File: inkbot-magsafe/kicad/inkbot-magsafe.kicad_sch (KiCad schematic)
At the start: 48 parts, among them J1 Panel FPC, U1 nRF52832-QFaa, U3 TPS22810DRV, U4 MIC5504-3.3, U5 BQ51050BRHL, Y1 32.768kHz, Y2 32MHz

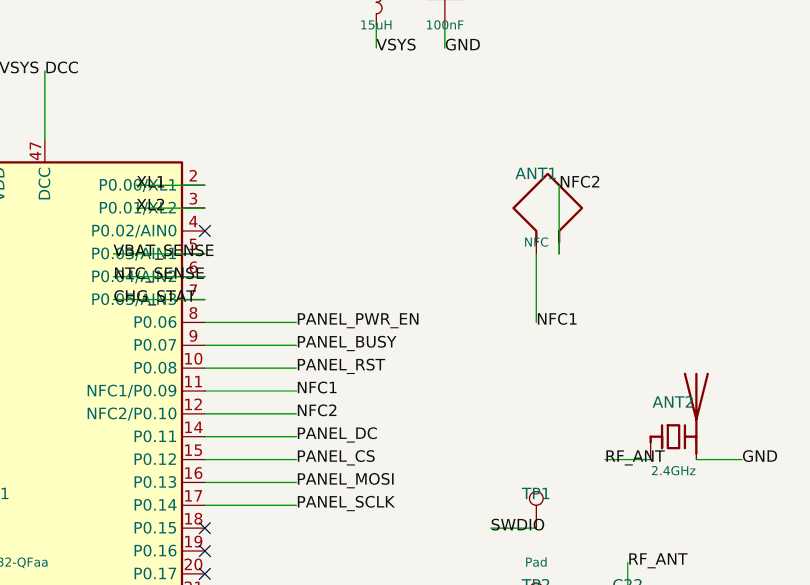
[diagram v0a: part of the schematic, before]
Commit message: inkbot-magsafe: drop NFC — pairing and frames are BLE-only
Remove the optional NFC loop antenna and free the nRF NFCT pins. Tap-to-pair
was never needed; BLE already carries pairing and the frame stream.

Co-authored-by: Jason Hall <imjasonh@users.noreply.github.com>
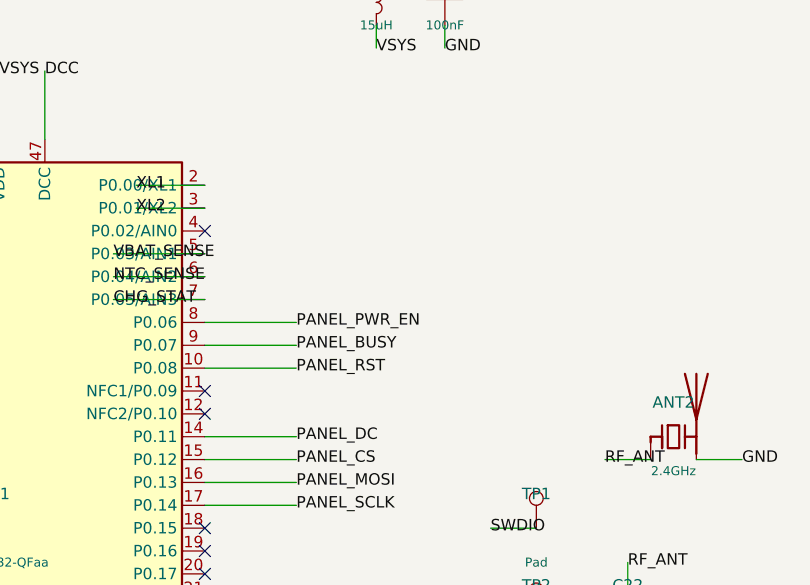
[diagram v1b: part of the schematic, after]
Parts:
- removed ANT1: NFC, symbol Device:Antenna_Loop
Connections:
- net NFC1: no longer names the net of U1.11 (NFC1/P0.09)
- net NFC2: no longer names the net of U1.12 (NFC2/P0.10)
- no-connect marks 17 -> 19

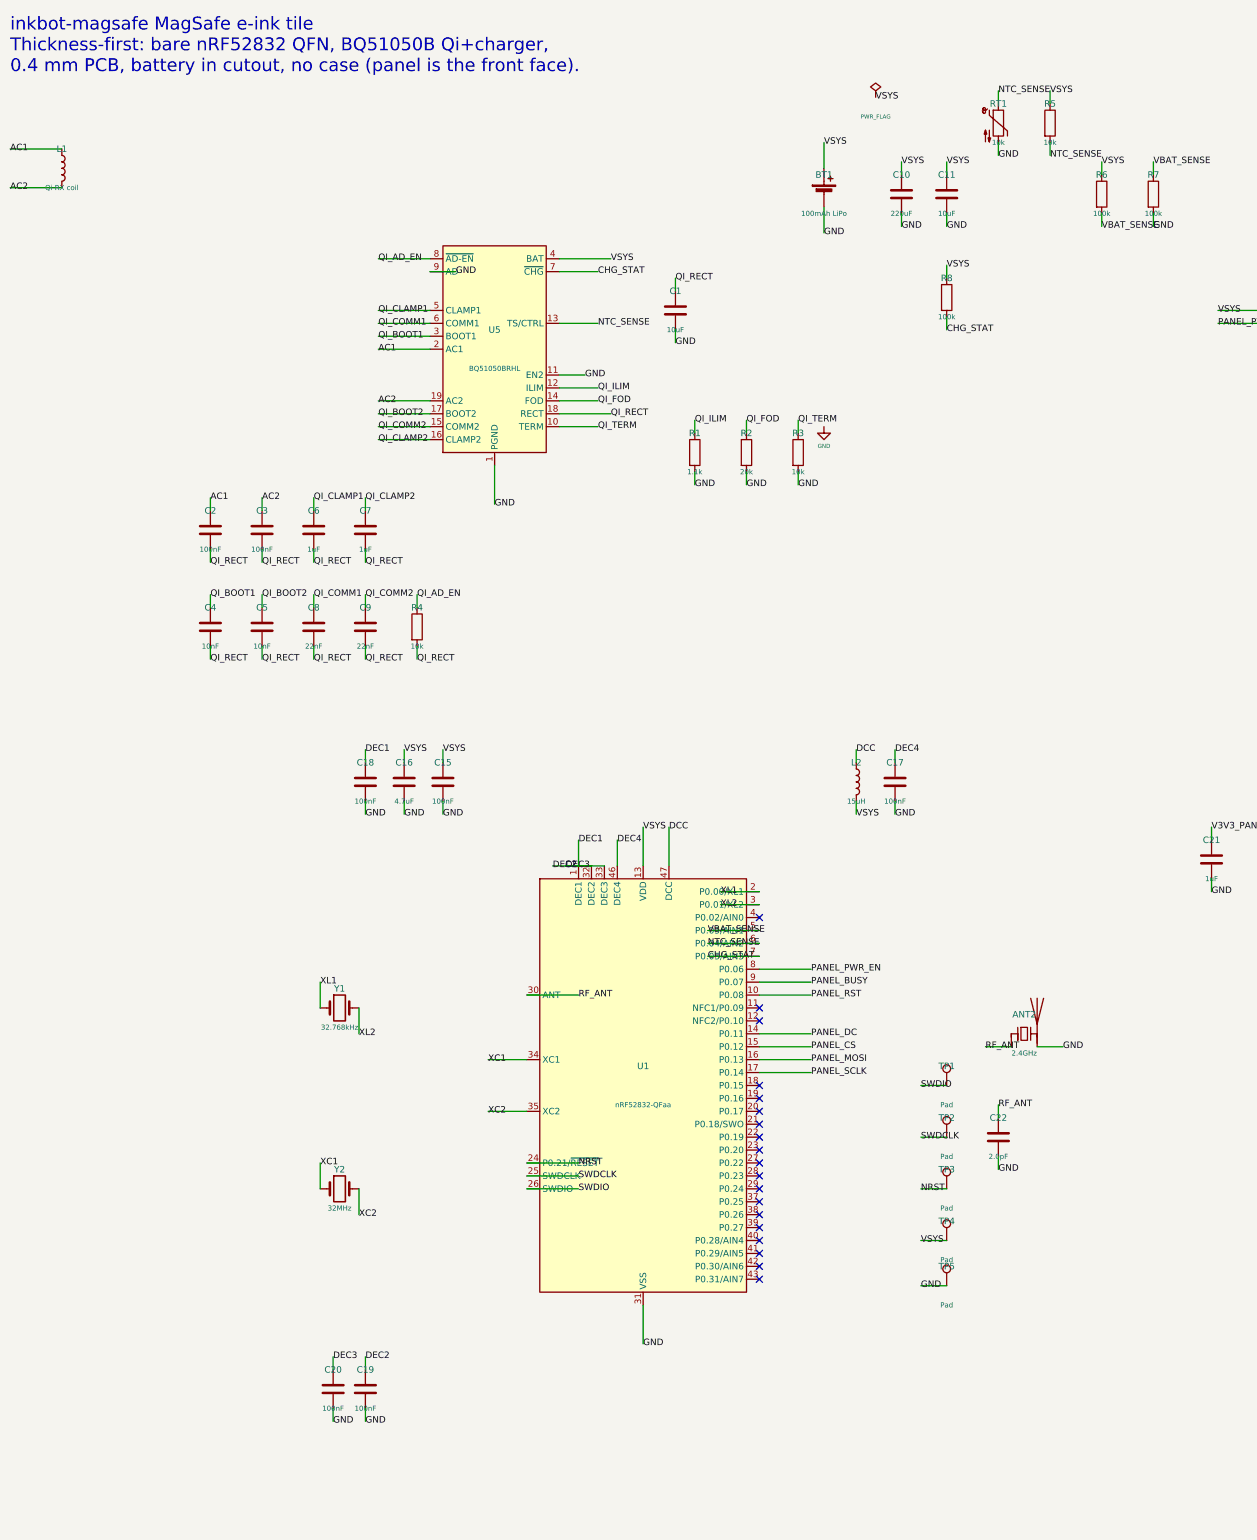
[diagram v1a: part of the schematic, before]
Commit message: inkbot-magsafe: 4.26in 480x800 panel + nRF52833; drop mini support
Maximize display for standard/Pro iPhones (minis dropped). Switch the panel to
the 4.26in GDEY0426T82 (480x800, SSD1677) — the largest mono e-paper that fits a
70.6mm iPhone in portrait — and the MCU to the nRF52833 (128KB RAM) to hold the
48KB framebuffer. Rework the schematic (QFN-40 pinout, verified netlist), the
board outline (66x108mm), firmware panel geometry, BOM, and docs. Add a phone
compatibility table to the design doc.

Co-authored-by: Jason Hall <imjasonh@users.noreply.github.com>
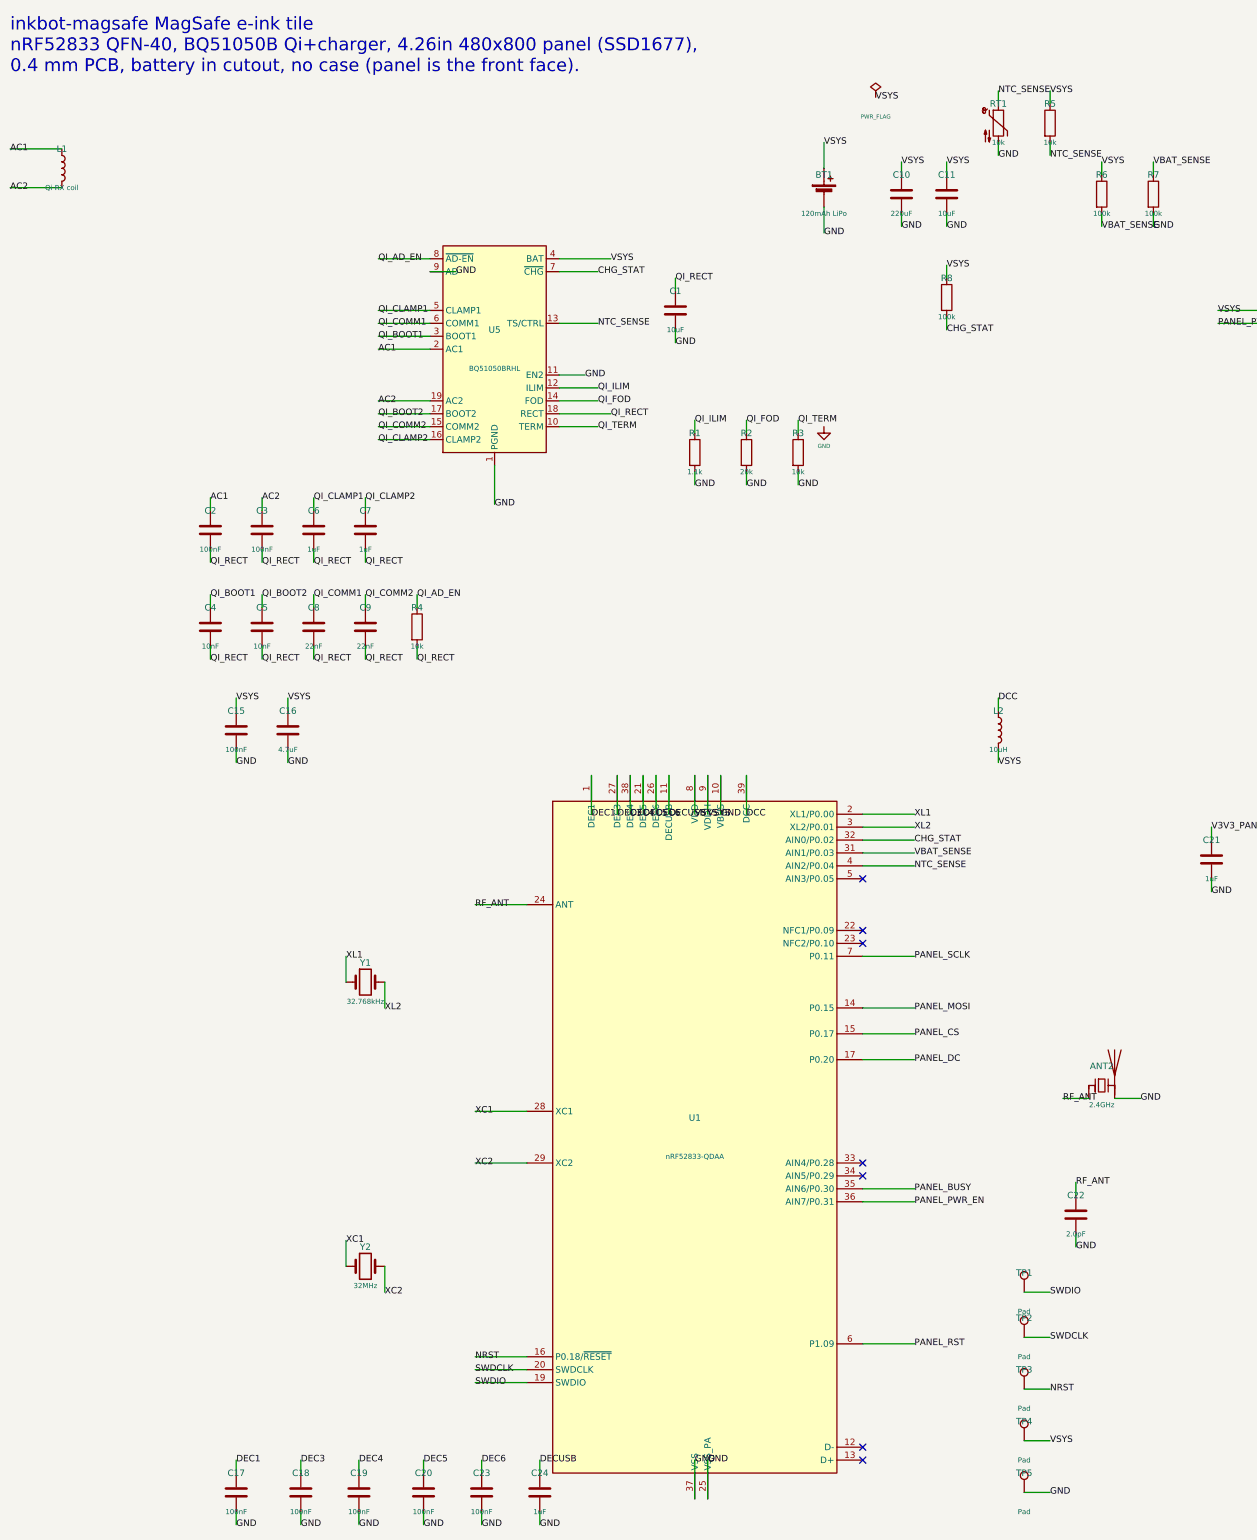
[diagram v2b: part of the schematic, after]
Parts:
- removed U1: nRF52832-QFaa, Package_DFN_QFN:QFN-48-1EP_6x6mm_P0.4mm_EP4.6x4.6mm, symbol MCU_Nordic:nRF52832-QFxx
- added C23: 100nF, Capacitor_SMD:C_0402_1005Metric, symbol Device:C
- added C24: 1uF, Capacitor_SMD:C_0402_1005Metric, symbol Device:C
- added U1: nRF52833-QDAA, Package_DFN_QFN:Nordic_QFN-40-1EP_5x5mm_P0.4mm, symbol MCU_Nordic:nRF52833_QDxx
- BT1: value 100mAh LiPo -> 120mAh LiPo
- L2: value 15uH -> 10uH
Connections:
- net CHG_STAT: now also U1.32 (AIN0/P0.02)
- net DCC: now also U1.39 (DCC)
- net DEC1: now also C17.1, U1.1 (DEC1); no longer C18.1
- net DEC4: now also C19.1, U1.38 (DEC4); no longer C17.1
- net GND: now also C23.2, C24.2, U1.10 (VBUS), U1.25 (VSS_PA), U1.37 (VSS), U1.41 (VSS)
- net NRST: now also U1.16 (P0.18/~{RESET})
- net NTC_SENSE: now also U1.4 (AIN2/P0.04)
- net PANEL_BUSY: now also U1.35 (AIN6/P0.30)
- net PANEL_CS: now also U1.15 (P0.17)
- net PANEL_DC: now also U1.17 (P0.20)
- net PANEL_MOSI: now also U1.14 (P0.15)
- net PANEL_PWR_EN: now also U1.36 (AIN7/P0.31)
- net PANEL_RST: now also U1.6 (P1.09)
- net PANEL_SCLK: now also U1.7 (P0.11)
- net RF_ANT: now also U1.24 (ANT)
- net SWDCLK: now also U1.20 (SWDCLK)
- net SWDIO: now also U1.19 (SWDIO)
- net VBAT_SENSE: now also U1.31 (AIN1/P0.03)
- net VSYS: now also U1.18 (VDD), U1.30 (VDD), U1.40 (VDD), U1.8 (VDD), U1.9 (VDDH)
- net XC1: now also U1.28 (XC1)
- net XC2: now also U1.29 (XC2)
- net XL1: now also U1.2 (XL1/P0.00)
- net XL2: now also U1.3 (XL2/P0.01)
- net DEC2 renamed DEC5
- net DEC5: now also U1.21 (DEC5); no longer C19.1
- new net DEC3: C18.1, U1.27 (DEC3)
- new net DEC6: C23.1, U1.26 (DEC6)
- new net DECUSB: C24.1, U1.11 (DECUSB)
- no-connect marks 19 -> 7
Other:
- note added: "inkbot-magsafe MagSafe e-ink tile nRF52833 QFN-40, BQ51050B Qi+charger, 4.26in 480x800 panel (SSD1677), 0.4 mm PCB, battery in cutout, no case (panel is the front face)."
- note removed: "inkbot-magsafe MagSafe e-ink tile Thickness-first: bare nRF52832 QFN, BQ51050B Qi+charger, 0.4 mm PCB, battery in cutout, no case (panel is the front face)."

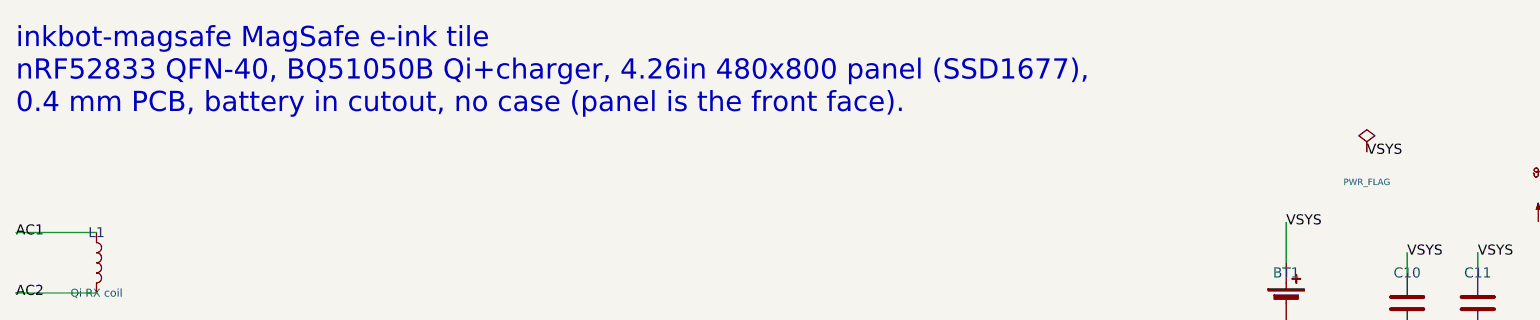
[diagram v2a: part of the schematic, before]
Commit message: inkbot-magsafe: drop 4.26in for 3.97in so it clears the phone bottom
The 4.26in module (105 mm tall) overhangs a 15 Pro by ~4 mm once the
MagSafe ring sits high enough to clear the cameras. Switch to the
GDEY0397T81P (56 x 97 mm, still 480x800 / SSD1677 / nRF52833) on a
60 x 99 mm board — ~5 mm bottom clearance on a 15 Pro.

Co-authored-by: Jason Hall <imjasonh@users.noreply.github.com>
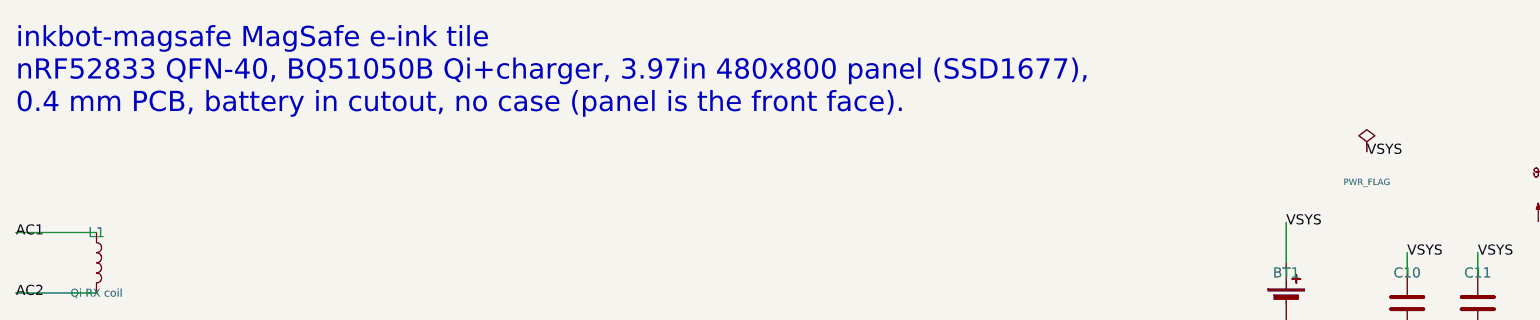
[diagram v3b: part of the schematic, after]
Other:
- note added: "inkbot-magsafe MagSafe e-ink tile nRF52833 QFN-40, BQ51050B Qi+charger, 3.97in 480x800 panel (SSD1677), 0.4 mm PCB, battery in cutout, no case (panel is the front face)."
- note removed: "inkbot-magsafe MagSafe e-ink tile nRF52833 QFN-40, BQ51050B Qi+charger, 4.26in 480x800 panel (SSD1677), 0.4 mm PCB, battery in cutout, no case (panel is the front face)."
